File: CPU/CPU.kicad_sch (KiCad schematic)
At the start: 211 parts, among them J1 Conn_02x36_Top_Bottom, P2 Conn_02x13_Top_Bottom, P3 Conn_02x13_Top_Bottom, P4 IDC-16, P5 Conn_02x25_Counter_Clockwise, P6 Conn_02x25_Counter_Clockwise, P7 Conn_02x07_Counter_Clockwise, P8 Conn_02x08_Odd_Even

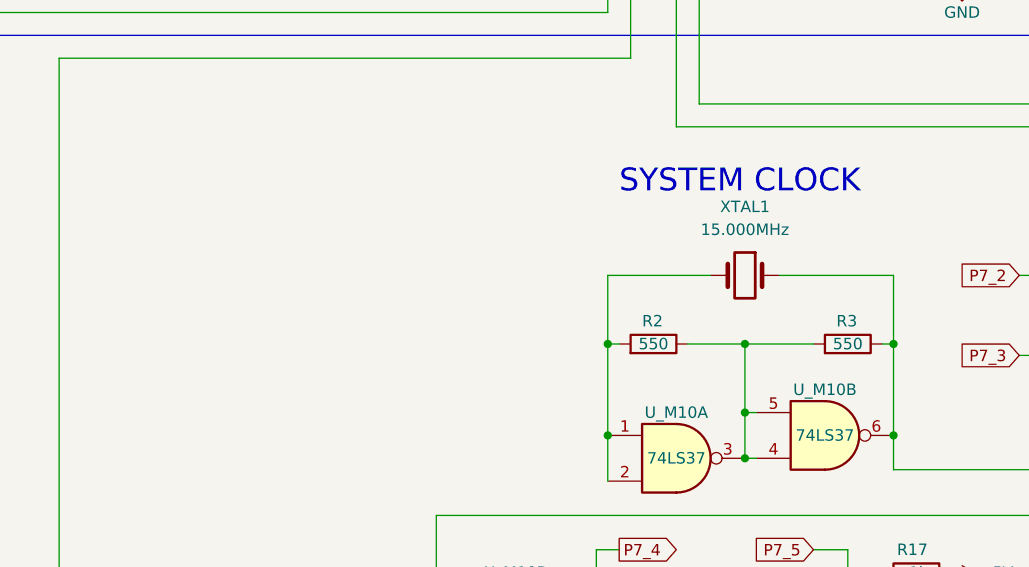
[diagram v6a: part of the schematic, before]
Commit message: CPU: Add important build info
Restructured the documentation, there's now one file per board. Easier to read
and maintain.
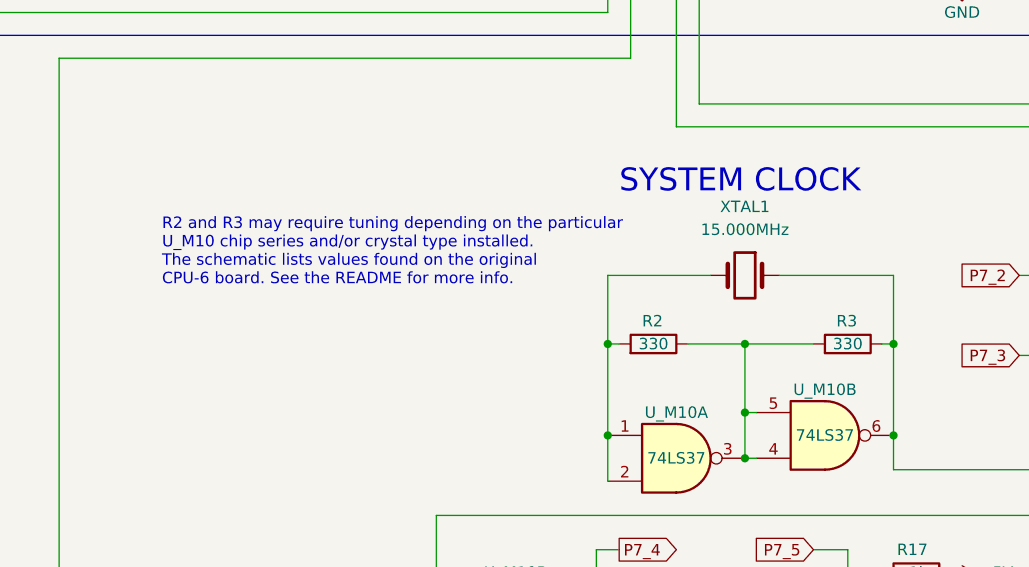
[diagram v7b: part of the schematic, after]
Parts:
- R2, R3: value 550 -> 330
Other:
- note added: "R2 and R3 may require tuning depending on the particular U_M10 chip series and/or crystal type installed. The schematic lists values found on the original CPU-6 board. See the README for more info."
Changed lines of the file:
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@@
     (effects (font (size 3.81 3.81)) (justify left bottom))
   )
+  (text "R2 and R3 may require tuning depending on the particular\nU_M10 chip series and/or crystal type installed.\nThe schematic lists values found on the original\nCPU-6 board. See the README for more info."
+    (at 839.47 307.34 0)
+    (effects (font (size 1.27 1.27)) (justify left bottom))
+  )
   (text "B12D is\nHIGH when REGFILE is addressed OR PTR.Q_{7} is set (high)\nLOW when Memory is addressed AND PTR.Q_{7} is clear (low)"
     (at 292.1 453.39 0)
@@
       (effects (font (size 1.27 1.27)) (justify left))
     )
-    (property "Value" "550" (id 1) (at 915.67 313.69 90))
+    (property "Value" "330" (id 1) (at 915.67 313.69 90))
     (property "Footprint" "Resistor_THT:R_Axial_DIN0207_L6.3mm_D2.5mm_P10.16mm_Horizontal" (id 2) (at 915.67 315.468 90)
       (effects (font (size 1.27 1.27)) hide)
@@
       (effects (font (size 1.27 1.27)) (justify left))
     )
-    (property "Value" "550" (id 1) (at 894.08 313.69 90))
+    (property "Value" "330" (id 1) (at 894.08 313.69 90))
     (property "Footprint" "Resistor_THT:R_Axial_DIN0207_L6.3mm_D2.5mm_P10.16mm_Horizontal" (id 2) (at 894.08 315.468 90)
       (effects (font (size 1.27 1.27)) hide)
@@
     )
     (path "/c4848a8c-ab6e-4ae9-9931-6b4bf2df301b"
-      (reference "R2") (unit 1) (value "550") (footprint "Resistor_THT:R_Axial_DIN0207_L6.3mm_D2.5mm_P10.16mm_Horizontal")
+      (reference "R2") (unit 1) (value "330") (footprint "Resistor_THT:R_Axial_DIN0207_L6.3mm_D2.5mm_P10.16mm_Horizontal")
     )
     (path "/5f53f0fc-ead6-45ba-a973-cead475b7028"
-      (reference "R3") (unit 1) (value "550") (footprint "Resistor_THT:R_Axial_DIN0207_L6.3mm_D2.5mm_P10.16mm_Horizontal")
+      (reference "R3") (unit 1) (value "330") (footprint "Resistor_THT:R_Axial_DIN0207_L6.3mm_D2.5mm_P10.16mm_Horizontal")
     )
     (path "/97b5092a-0879-45ef-a2ec-d360c06c0691"
